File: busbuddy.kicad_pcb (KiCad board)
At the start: 2 copper layers, 45 parts, among them J201 1054500101, J301 Conn_01x07_Pin, J302 Conn_01x07_Pin, J401 FH12A-24S-0.5SH(55), Q201 S8050, Q202 S8050, Q401 Q_NMOS_GSD, SW301 TS-1088R-02026, SW302 TS-1088R-02026, U201 CH340G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

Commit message: Remove CH340G
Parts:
- removed C203: 100n, Capacitor_SMD:C_0805_2012Metric
- removed U201: CH340G, Package_SO:SOIC-16_3.9x9.9mm_P1.27mm
- added C206: 4u7, Capacitor_SMD:C_0805_2012Metric, F.Cu at (111.2, 46.9)
- added C207: 4u7, Capacitor_SMD:C_0805_2012Metric, F.Cu at (111.2, 49.9)
- added C208: 100n, Capacitor_SMD:C_0805_2012Metric, F.Cu at (111.2, 52.9)
- added D201: SP0503BAHT, Package_TO_SOT_SMD:SOT-143, F.Cu at (115.5, 54.0)
- added U202: CP2104, Package_DFN_QFN:QFN-24-1EP_4x4mm_P0.5mm_EP2.6x2.6mm, F.Cu at (116.5, 48.5)
- C201: value 10u -> 5u
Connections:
- C201 pad 1: /USB/5V -> /USB/VIO
- J201 pad S1: GND -> Net-(D201-A)

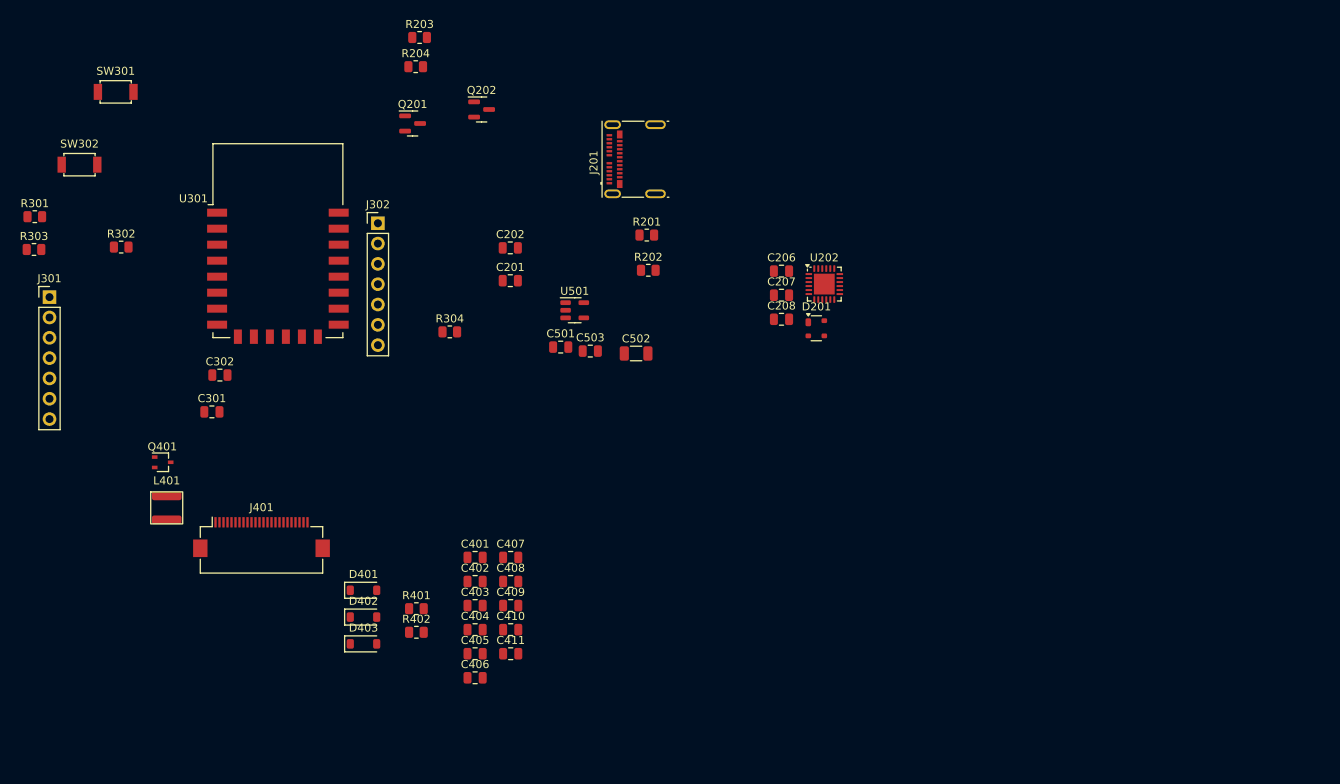
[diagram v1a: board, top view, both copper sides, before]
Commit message: Switch to 16 pin USB-C
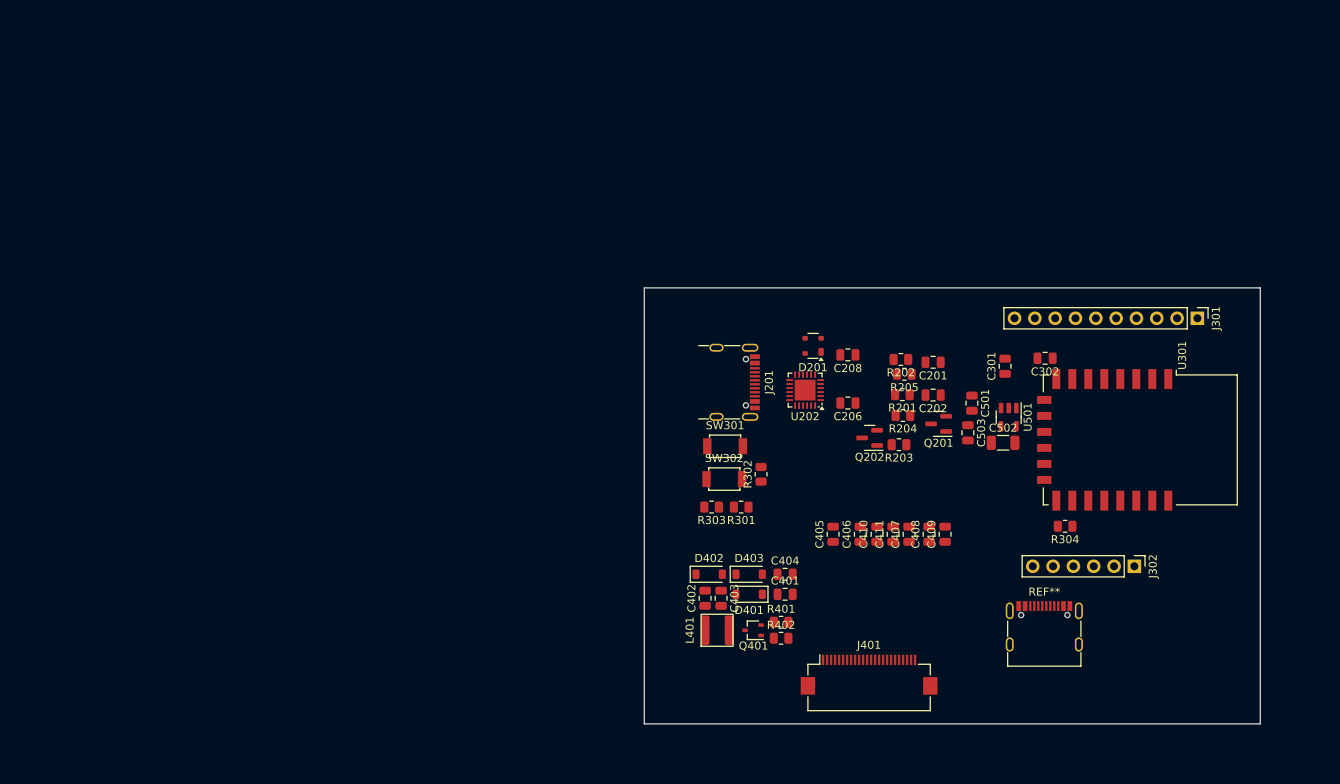
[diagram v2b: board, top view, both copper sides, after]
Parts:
- removed C207: 4u7, Capacitor_SMD:C_0805_2012Metric
- added R205: 4k7, Resistor_SMD:R_0805_2012Metric, F.Cu at (126.5, 59.8)
- added REF**: USB_C_Receptacle_G-Switch_GT-USB-7010ASV, Connector_USB:USB_C_Receptacle_G-Switch_GT-USB-7010ASV, F.Cu at (144.0, 92.5)
- J201: footprint busbuddy:USB_C_Receptacle_Molex_105450-0101 -> busbuddy:USB_C_Receptacle_G-Switch_GT-USB-7010ASV
- J301: value Conn_01x07_Pin -> Conn_01x05_Pin; footprint Connector_PinHeader_2.54mm:PinHeader_1x07_P2.54mm_Vertical -> Connector_PinHeader_2.54mm:PinHeader_1x10_P2.54mm_Vertical
- J302: footprint Connector_PinHeader_2.54mm:PinHeader_1x07_P2.54mm_Vertical -> Connector_PinHeader_2.54mm:PinHeader_1x06_P2.54mm_Vertical
- moved J301 143.5 mm to (163.1, 52.8), turned to -90 degrees
- moved U301 110.6 mm to (156.0, 68.0), turned to -90 degrees
- moved J302 103.8 mm to (155.3, 83.8), turned to -90 degrees
- moved C302 103.2 mm to (144.1, 57.8), turned to 180 degrees
- moved C301 99.3 mm to (139.1, 58.8), turned to 90 degrees
- moved R301 95.5 mm to (106.1, 76.4), turned to 180 degrees
- moved R303 90.6 mm to (102.4, 76.4), turned to 180 degrees
- moved SW302 89.7 mm to (104.0, 72.9)
- moved SW301 88.1 mm to (104.1, 68.8)
- moved R302 84.9 mm to (108.6, 72.3), turned to 90 degrees
- moved R304 80.7 mm to (146.6, 78.8), turned to 180 degrees
- moved R203 78.6 mm to (125.8, 68.6), turned to 180 degrees
- moved J401 77.9 mm to (122.1, 97.3)
- moved Q401 76.7 mm to (107.6, 91.8), turned to 180 degrees
- moved Q201 75.7 mm to (130.8, 66.0), turned to 180 degrees
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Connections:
- J301 pad 1: unconnected-(J301-Pin_1-Pad1) -> /MCU/~{RST}
- J301 pad 2: unconnected-(J301-Pin_2-Pad2) -> /MCU/ADC
- J301 pad 3: unconnected-(J301-Pin_3-Pad3) -> /MCU/EN
- J301 pad 4: unconnected-(J301-Pin_4-Pad4) -> /MCU/GPIO16
- J301 pad 5: unconnected-(J301-Pin_5-Pad5) -> /MCU/GPIO14
- J301 pad 6: unconnected-(J301-Pin_6-Pad6) -> /MCU/GPIO12
- J301 pad 7: unconnected-(J301-Pin_7-Pad7) -> /MCU/GPIO13
- J302 pad 1: unconnected-(J302-Pin_1-Pad1) -> /MCU/GPIO5
- J302 pad 2: unconnected-(J302-Pin_2-Pad2) -> /MCU/GPIO4
- J302 pad 3: unconnected-(J302-Pin_3-Pad3) -> /MCU/GPIO0
- J302 pad 4: unconnected-(J302-Pin_4-Pad4) -> /MCU/GPIO2
- J302 pad 5: unconnected-(J302-Pin_5-Pad5) -> /MCU/GPIO15
- J302 pad 6: unconnected-(J302-Pin_6-Pad6) -> /MCU/GPIO10
- R303 pad 1: Net-(U301-EN) -> /MCU/EN
- R304 pad 1: Net-(U301-GPIO15) -> /MCU/GPIO15
- U301 pad 16: Net-(U301-GPIO15) -> /MCU/GPIO15
- U301 pad 3: Net-(U301-EN) -> /MCU/EN
- U301 pad 5: /MCU/GPIO8 -> /MCU/GPIO14
- U301 pad 6: /MCU/GPIO6 -> /MCU/GPIO12
- U301 pad 7: /MCU/GPIO7 -> /MCU/GPIO13
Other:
- board outline added: 77 x 54.5 mm

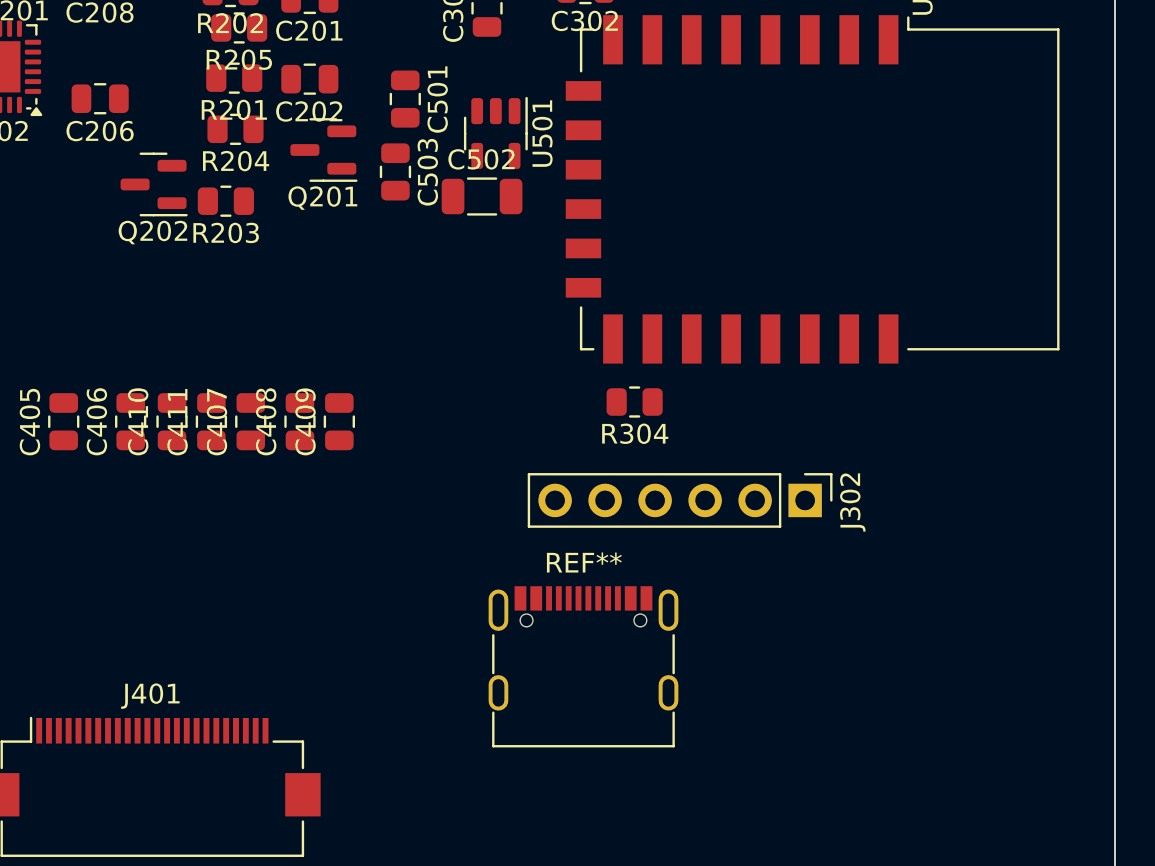
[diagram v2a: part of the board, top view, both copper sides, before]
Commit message: Correct SPI pinout
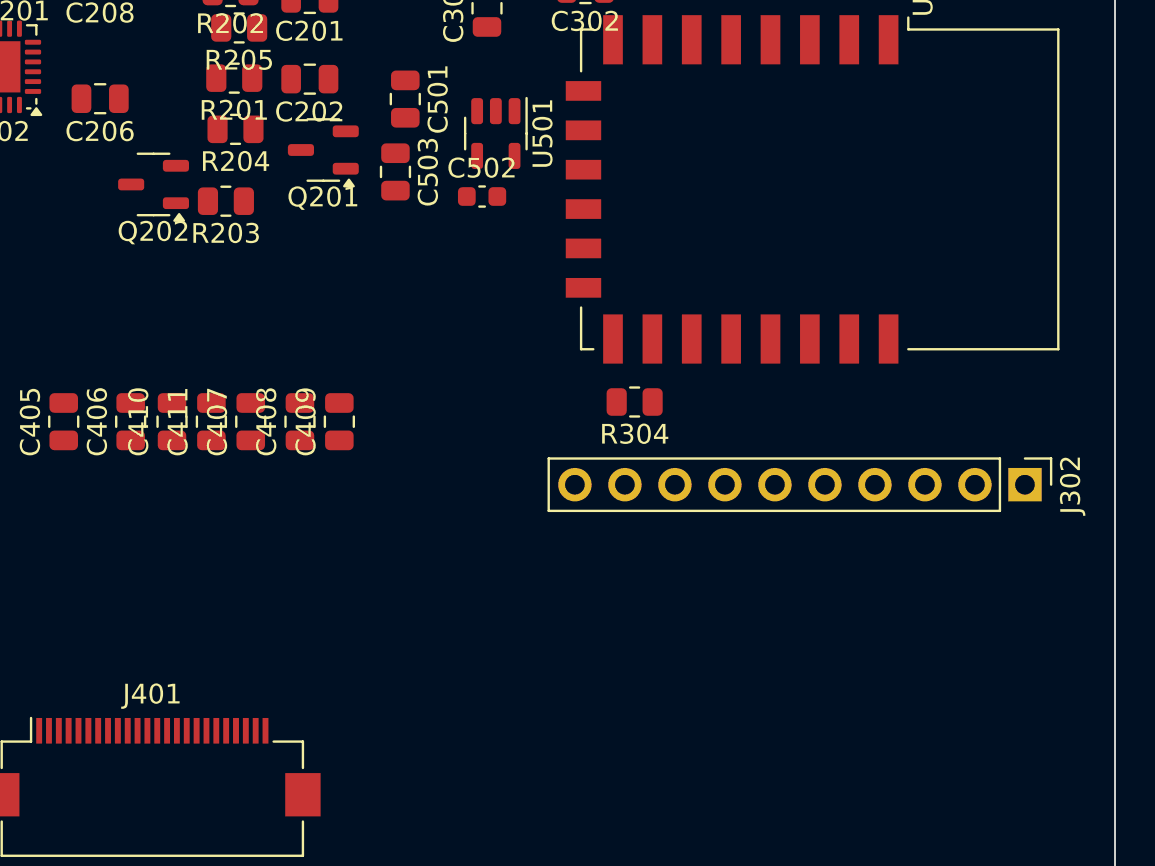
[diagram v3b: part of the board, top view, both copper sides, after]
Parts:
- removed REF**: USB_C_Receptacle_G-Switch_GT-USB-7010ASV, Connector_USB:USB_C_Receptacle_G-Switch_GT-USB-7010ASV
- C502: value 470p -> 10n; footprint Capacitor_SMD:C_1206_3216Metric -> Capacitor_SMD:C_0603_1608Metric
- J201: value 1054500101 -> GT-USB-7010ASV
- J302: value Conn_01x07_Pin -> Conn_01x10_Pin; footprint Connector_PinHeader_2.54mm:PinHeader_1x06_P2.54mm_Vertical -> Connector_PinHeader_2.54mm:PinHeader_1x10_P2.54mm_Vertical
- Q201, Q202: footprint Package_TO_SOT_SMD:SOT-23 -> Package_TO_SOT_SMD:SOT-23-3
- moved J302 11.2 mm to (166.4, 83.0)
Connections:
- J301 pad 5: /MCU/GPIO14 -> /EPD/SPI.SCLK
- J301 pad 7: /MCU/GPIO13 -> /EPD/SPI.MOSI
- J302 pad 2: /MCU/GPIO4 -> /EPD/EPD_BUSY
- J302 pad 3: /MCU/GPIO0 -> /EPD/EPD_D/C
- J302 pad 4: /MCU/GPIO2 -> /EPD/EPD_RST
- J302 pad 5: /MCU/GPIO15 -> /EPD/SPI.~{CS}
- J401 pad 10: /EPD/RES -> /EPD/EPD_RST
- J401 pad 11: /EPD/D/C -> /EPD/EPD_D/C
- J401 pad 12: /EPD/~{CS} -> /EPD/SPI.~{CS}
- J401 pad 13: /EPD/SCLK -> /EPD/SPI.SCLK
- J401 pad 14: /EPD/MOSI -> /EPD/SPI.MOSI
- J401 pad 15: +3.3V -> /EPD/3V3
- J401 pad 16: +3.3V -> /EPD/3V3
- J401 pad 21: /EPD/VGH -> /EPD/PREVGH
- J401 pad 23: /EPD/VGL -> /EPD/PREVGL
- J401 pad 6: /EPD/TSCL -> unconnected-(J401-TSCL-Pad6)
- J401 pad 7: /EPD/TSDA -> unconnected-(J401-TSDA-Pad7)
- J401 pad 8: /EPD/BS -> GND
- J401 pad 9: /EPD/BUSY -> /EPD/EPD_BUSY
- Q202 pad 3: /MCU/GPIO0 -> /EPD/EPD_D/C
- R302 pad 2: /MCU/GPIO0 -> /EPD/EPD_D/C
- R304 pad 1: /MCU/GPIO15 -> /EPD/SPI.~{CS}
- SW302 pad 2: /MCU/GPIO0 -> /EPD/EPD_D/C
- U301 pad 10: /EPD/MISO -> /MCU/MISO
- U301 pad 13: /EPD/MOSI -> /MCU/MOSI
- U301 pad 14: /EPD/SCLK -> /MCU/SCLK
- U301 pad 16: /MCU/GPIO15 -> /EPD/SPI.~{CS}
- U301 pad 17: /MCU/GPIO2 -> /EPD/EPD_RST
- U301 pad 18: /MCU/GPIO0 -> /EPD/EPD_D/C
- U301 pad 19: /MCU/GPIO4 -> /EPD/EPD_BUSY
- U301 pad 5: /MCU/GPIO14 -> /EPD/SPI.SCLK
- U301 pad 7: /MCU/GPIO13 -> /EPD/SPI.MOSI
- U301 pad 9: /EPD/~{CS} -> /MCU/CS0

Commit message: Finish everything
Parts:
- C201: value 5u -> 4u7
- J301: footprint Connector_PinHeader_2.54mm:PinHeader_1x10_P2.54mm_Vertical -> Connector_PinHeader_2.54mm:PinHeader_1x12_P2.54mm_Vertical
- moved J301 66.2 mm to (97.0, 55.7), turned to 0 degrees
- moved J302 49.8 mm to (125.0, 55.3), turned to 0 degrees
- moved U301 45.8 mm to (111.0, 59.3), turned to 0 degrees
- moved J201 45.5 mm to (149.0, 68.0), turned to 90 degrees
- moved C302 44.1 mm to (103.0, 73.8), turned to 0 degrees
- moved C301 39.9 mm to (103.0, 75.8), turned to 0 degrees
- moved SW302 35.3 mm to (138.0, 82.5), turned to 90 degrees
- moved U501 33.8 mm to (111.0, 83.3), turned to 180 degrees
- moved SW301 32.9 mm to (134.0, 82.5), turned to 90 degrees
- moved C503 31.4 mm to (107.5, 83.3), turned to 90 degrees
- moved C502 30.5 mm to (111.0, 80.8), turned to 180 degrees
- moved R302 29.8 mm to (137.8, 78.2), turned to 0 degrees
- moved D201 28.9 mm to (141.5, 68.0), turned to 0 degrees
- moved C501 28.5 mm to (114.5, 83.3), turned to 90 degrees
- moved R301 28.2 mm to (134.2, 78.2), turned to 0 degrees
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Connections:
- net Net-(D201-A) renamed /USB/SHIELD
- net Net-(J201-CC1) renamed /USB/CC1
- net Net-(J201-CC2) renamed /USB/CC2
- net Net-(U202-VPP) renamed /USB/VPP
- net Net-(U202-~{RST}) renamed /USB/CP2104_~{RST}
- net Net-(U501-BP) renamed /LDO/BYP
- D201 pad 2: /USB/D+ -> /USB/D-
- D201 pad 3: /USB/D- -> /USB/D+
- J301 pad 10: GND -> /MCU/CS0
- J301 pad 5: /EPD/SPI.SCLK -> /MCU/GPIO12
- J301 pad 6: /MCU/GPIO12 -> /EPD/SPI.MOSI
- J301 pad 7: /EPD/SPI.MOSI -> /EPD/SPI.SCLK
- J301 pad 8: /MCU/GPIO9 -> /EPD/3V3
- J301 pad 9: /EPD/3V3 -> GND
- J302 pad 1: /MCU/GPIO5 -> /MCU/TXD
- J302 pad 10: /MCU/SCLK -> /MCU/GPIO10
- J302 pad 2: /EPD/EPD_BUSY -> /MCU/RXD
- J302 pad 3: /EPD/EPD_D/C -> /MCU/GPIO5
- J302 pad 4: /EPD/EPD_RST -> /EPD/EPD_BUSY
- J302 pad 5: /EPD/SPI.~{CS} -> /EPD/EPD_RST
- J302 pad 6: /MCU/GPIO10 -> /EPD/EPD_D/C
- J302 pad 7: /MCU/CS0 -> /EPD/SPI.~{CS}
- J302 pad 8: /MCU/MISO -> /MCU/SCLK
- J401 pad 1: unconnected-(J401-NC-Pad1) -> /EPD/VCOM
- J401 pad 10: /EPD/EPD_RST -> /EPD/3V3
- J401 pad 11: /EPD/EPD_D/C -> /EPD/SPI.MOSI
- J401 pad 12: /EPD/SPI.~{CS} -> /EPD/SPI.SCLK
- J401 pad 13: /EPD/SPI.SCLK -> /EPD/SPI.~{CS}
- J401 pad 14: /EPD/SPI.MOSI -> /EPD/EPD_D/C
- J401 pad 15: /EPD/3V3 -> /EPD/EPD_RST
- J401 pad 16: /EPD/3V3 -> /EPD/EPD_BUSY
- J401 pad 18: /EPD/VDD -> unconnected-(J401-TSDA-Pad18)
- J401 pad 19: /EPD/VPP -> unconnected-(J401-TSCL-Pad19)
- J401 pad 2: /EPD/GDR -> /EPD/PREVGL
- J401 pad 20: /EPD/VSH1 -> /EPD/VSH2
- J401 pad 21: /EPD/PREVGH -> unconnected-(J401-NC-Pad21)
- J401 pad 22: /EPD/VSL -> /EPD/RESE
- J401 pad 23: /EPD/PREVGL -> /EPD/GDR
- J401 pad 24: /EPD/VCOM -> unconnected-(J401-NC-Pad24)
- J401 pad 3: /EPD/RESE -> /EPD/VSL
- J401 pad 4: unconnected-(J401-NC-Pad4) -> /EPD/PREVGH
- J401 pad 5: /EPD/VSH2 -> /EPD/VSH1
- J401 pad 6: unconnected-(J401-TSCL-Pad6) -> /EPD/VPP
- J401 pad 7: unconnected-(J401-TSDA-Pad7) -> /EPD/VDD
- J401 pad 9: /EPD/EPD_BUSY -> /EPD/3V3
- U202 pad 20: /MCU/RXD -> /MCU/TXD
- U202 pad 21: /MCU/TXD -> /MCU/RXD
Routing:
- net /EPD/3V3: track 0.00 -> 121.3 mm, vias 0 -> 5
- net /EPD/EPD_D/C: track 0.00 -> 71.8 mm, vias 0 -> 1
- net /EPD/SPI.SCLK: track 0.00 -> 69.8 mm
- net /USB/5V: track 0.00 -> 67.0 mm, vias 0 -> 4
- net /EPD/SPI.MOSI: track 0.00 -> 64.3 mm
- net /MCU/~{RST}: track 0.00 -> 64.1 mm, vias 0 -> 1
- net /EPD/EPD_BUSY: track 0.00 -> 52.6 mm
- net /EPD/EPD_RST: track 0.00 -> 47.5 mm
- net /EPD/SPI.~{CS}: track 0.00 -> 41.6 mm
- net GND: track 0.00 -> 35.7 mm, vias 0 -> 40
- net /EPD/GDR: track 0.00 -> 25.9 mm
- net /USB/SHIELD: track 0.00 -> 24.9 mm, vias 0 -> 1
- net /EPD/RESE: track 0.00 -> 22.0 mm
- net /MCU/GPIO9: track 0.00 -> 20.0 mm, vias 0 -> 1
- net /USB/D-: track 0.00 -> 19.8 mm, vias 0 -> 2
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- added copper zone on F.Cu, net /USB/5V
- added copper zone on F.Cu, net /USB/VIO
- added copper zone on B.Cu, net GND
- added copper zone on F.Cu, net GND
- added copper zone on In1.Cu, net GND
- added copper zone on In2.Cu, net GND
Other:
- board size 77 x 54.5 mm -> 60 x 53 mm
- copper layers 2 -> 4
- board text added: "3V3"
- board text added: "ADC"
- board text added: "CS0"
- board text added: "EN"
- board text added: "EPD Driver Rev A © 2024 Marcel Robitaille"
- board text added: "GND"
- board text added: "GPIO0"
- board text added: "IO0"
- board text added: "IO1"
- board text added: "IO10"
- board text added: "IO12"
- board text added: "IO13"
- board text added: "IO14"
- board text added: "IO15"
- board text added: "IO16"
- board text added: "IO2"
- board text added: "IO3"
- board text added: "IO4"
- board text added: "IO5"
- board text added: "IO9"
- board text added: "MISO"
- board text added: "MOSI"
- board text added: "RST"
- board text added: "SCLK"
